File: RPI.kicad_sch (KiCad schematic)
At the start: 29 parts, among them J1 Conn_01x02_Male, J2 GPIO, J3 Conn_02x12, J4 Conn_02x12, J5 Conn_01x06, J6 Conn_01x04, J7 Conn_01x03, J8 Conn_01x02, J9 Conn_01x02, Q1 BC856BDW1, Q1 IRF9540N, Q2 IRF9540N, SW1 SW_SPDT, SW2 SW_SPDT, U1 LM1085-ADJ

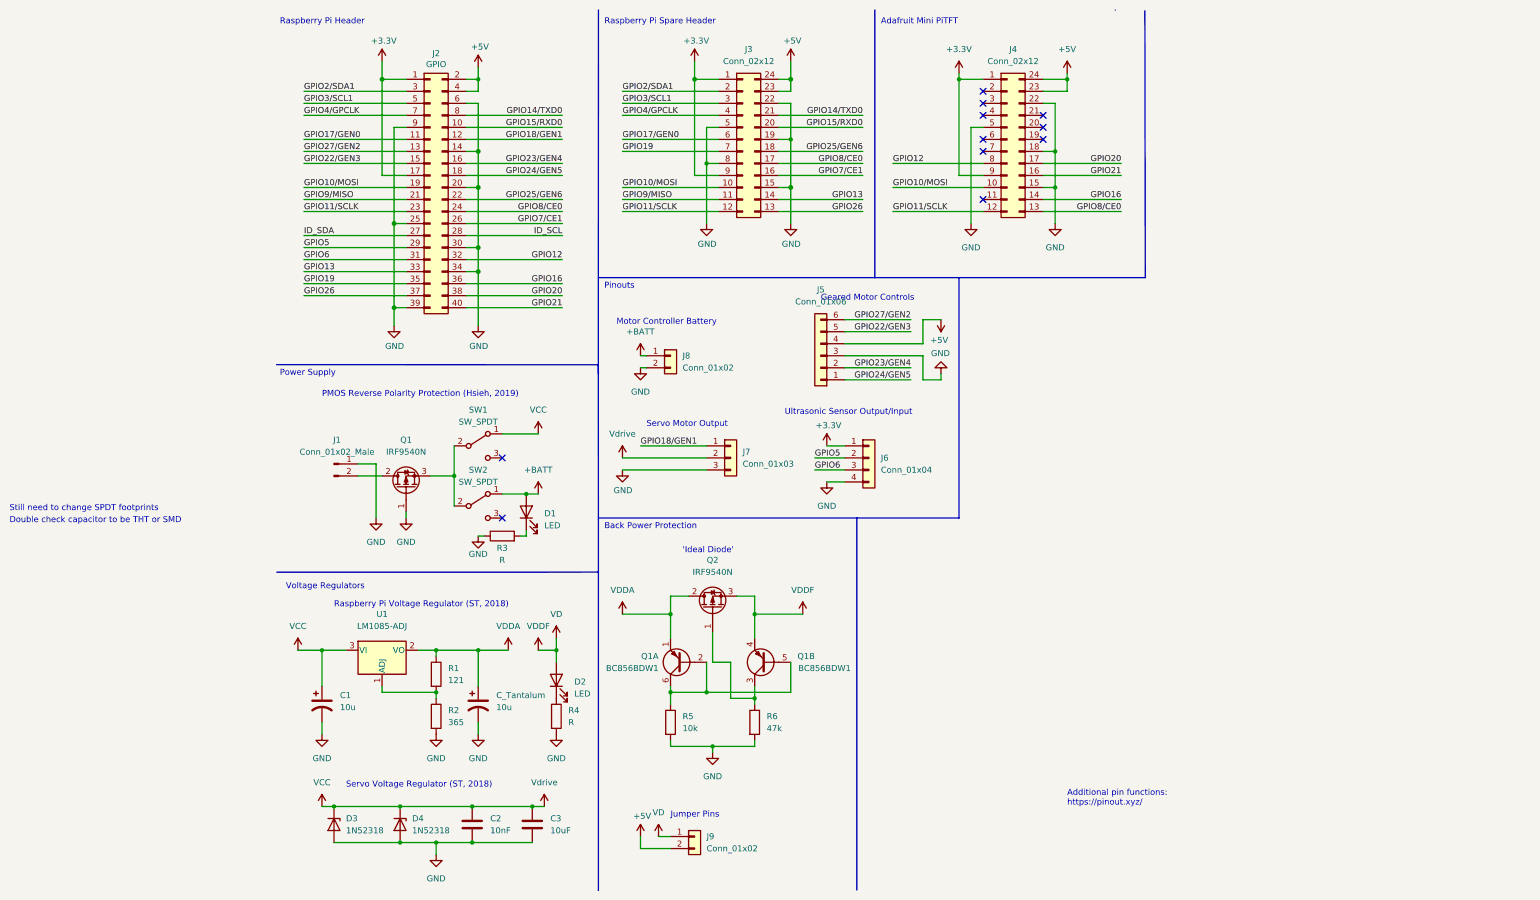
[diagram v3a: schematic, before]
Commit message: Completed Schematic, just need to edit footprints
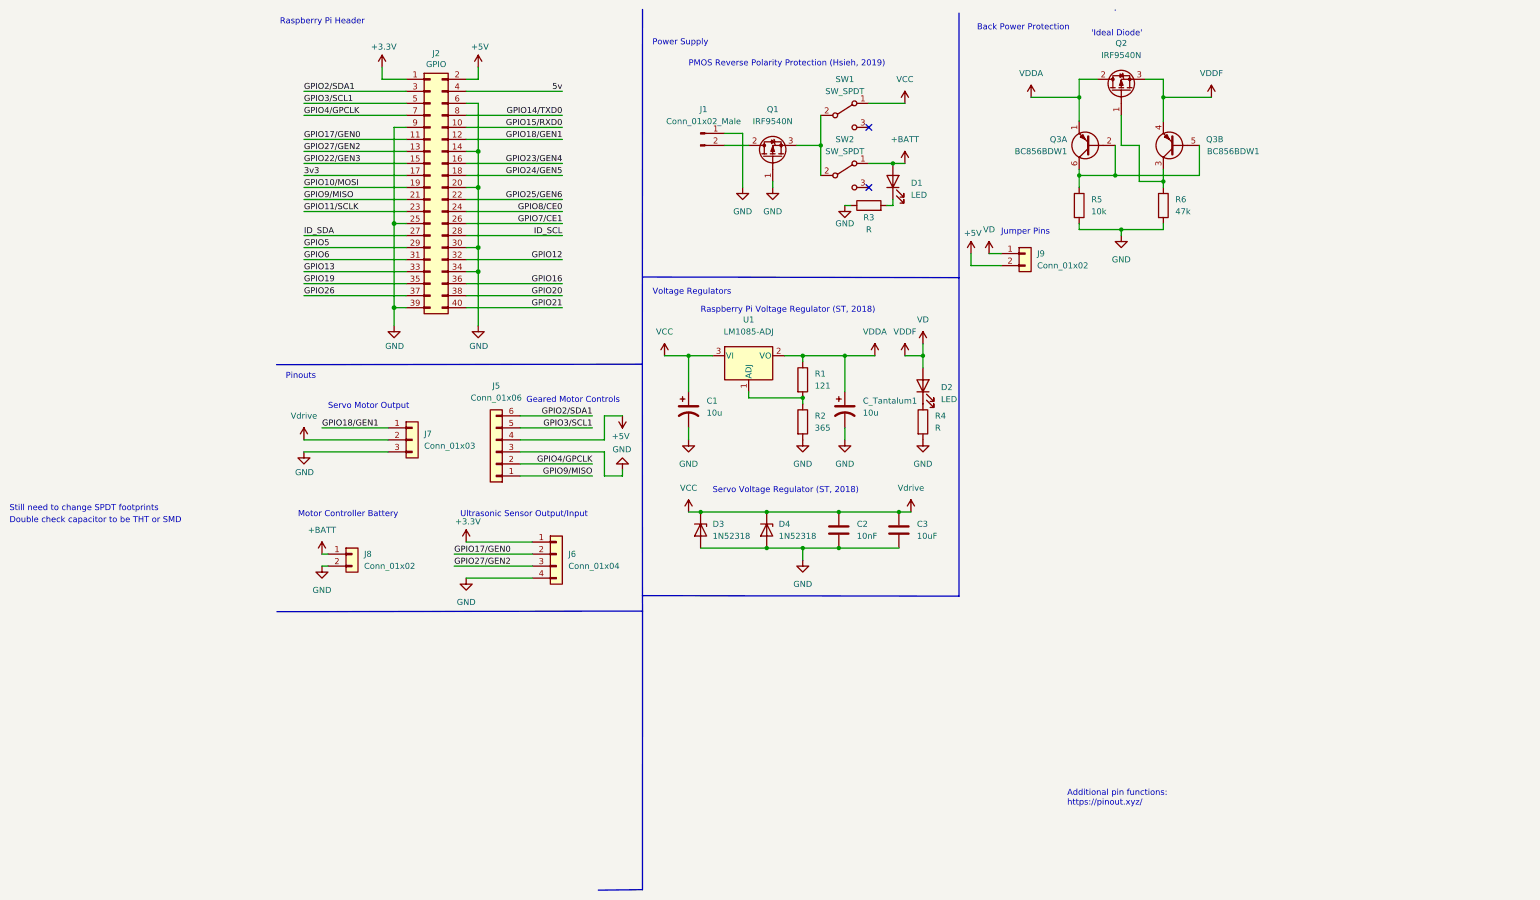
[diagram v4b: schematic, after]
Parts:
- removed J3, J4: Conn_02x12, Connector_PinSocket_2.54mm:PinSocket_2x12_P2.54mm_Vertical, symbol Connector_Generic:Conn_02x12_Counter_Clockwise
- C1: footprint (none) -> Capacitor_THT:CP_Radial_D5.0mm_P2.50mm
- C2, C3: footprint (none) -> Capacitor_SMD:C_0805_2012Metric_Pad1.18x1.45mm_HandSolder
- C_Tantalum1: renamed from C_Tantalum; footprint (none) -> Capacitor_Tantalum_SMD:CP_EIA-2012-12_Kemet-R_Pad1.30x1.05mm_HandSolder
- SW1, SW2: footprint (none) -> RPi_Hat:Switch_SPDT_Jaycar
- U1: footprint (none) -> RPi_Hat:LM1085-5.0
- renumbered Q1 to Q3
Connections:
- net +3V3: no longer J2.17 (Pin_17)
- net +5V: no longer J2.4 (Pin_4)
- net GPIO17/GEN0: now also J6.2 (Pin_2)
- net GPIO22/GEN3: no longer J5.5 (Pin_5)
- net GPIO23/GEN4: no longer J5.2 (Pin_2)
- net GPIO24/GEN5: no longer J5.1 (Pin_1)
- net GPIO27/GEN2: now also J6.3 (Pin_3); no longer J5.6 (Pin_6)
- net GPIO2/SDA1: now also J5.6 (Pin_6)
- net GPIO3/SCL1: now also J5.5 (Pin_5)
- net GPIO4/GPCLK: now also J5.2 (Pin_2)
- net GPIO5: no longer J6.2 (Pin_2)
- net GPIO6: no longer J6.3 (Pin_3)
- net GPIO9/MISO: now also J5.1 (Pin_1)
- new net 3v3: J2.17 (Pin_17)
- new net 5v: J2.4 (Pin_4)
- no-connect marks 11 -> 2
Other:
- note removed: "Adafruit Mini PiTFT"
- note removed: "Raspberry Pi Spare Header"
- moved on the sheet: C1, C2, C3, C_Tantalum1, D1, D2, D3, D4, J1, J5, J6, J7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

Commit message: Official completion (Maybe add Gerald in)
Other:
- note removed: "Double check capacitor to be THT or SMD"
- note removed: "Still need to change SPDT footprints"
- moved on the sheet: J7, J9, Q2, Q3A, Q3B, R5, R6

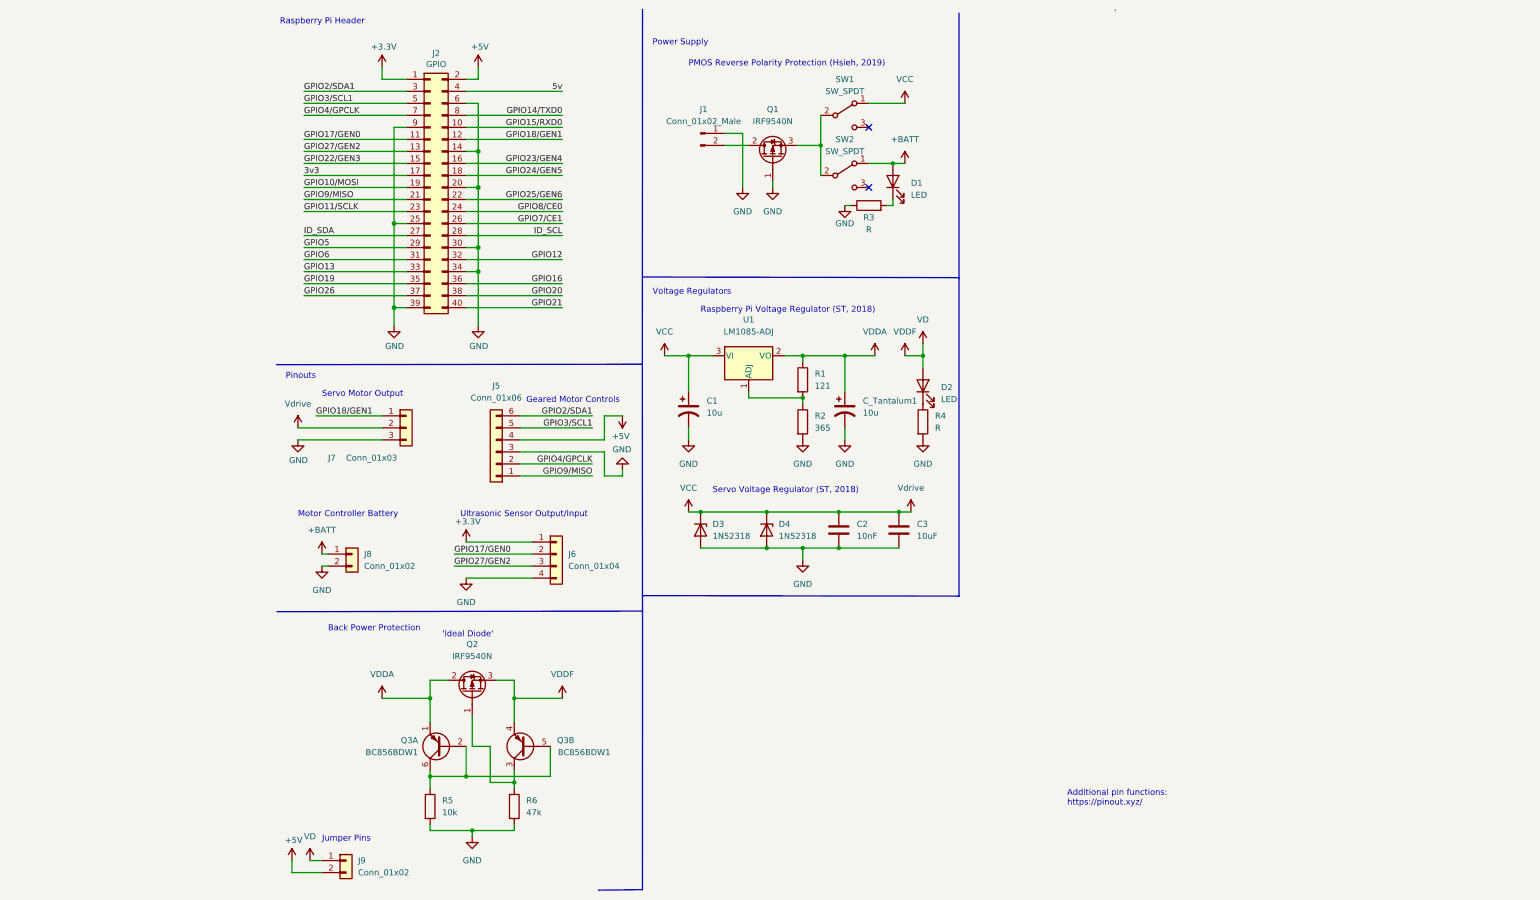
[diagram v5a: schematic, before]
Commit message: Added Fuse
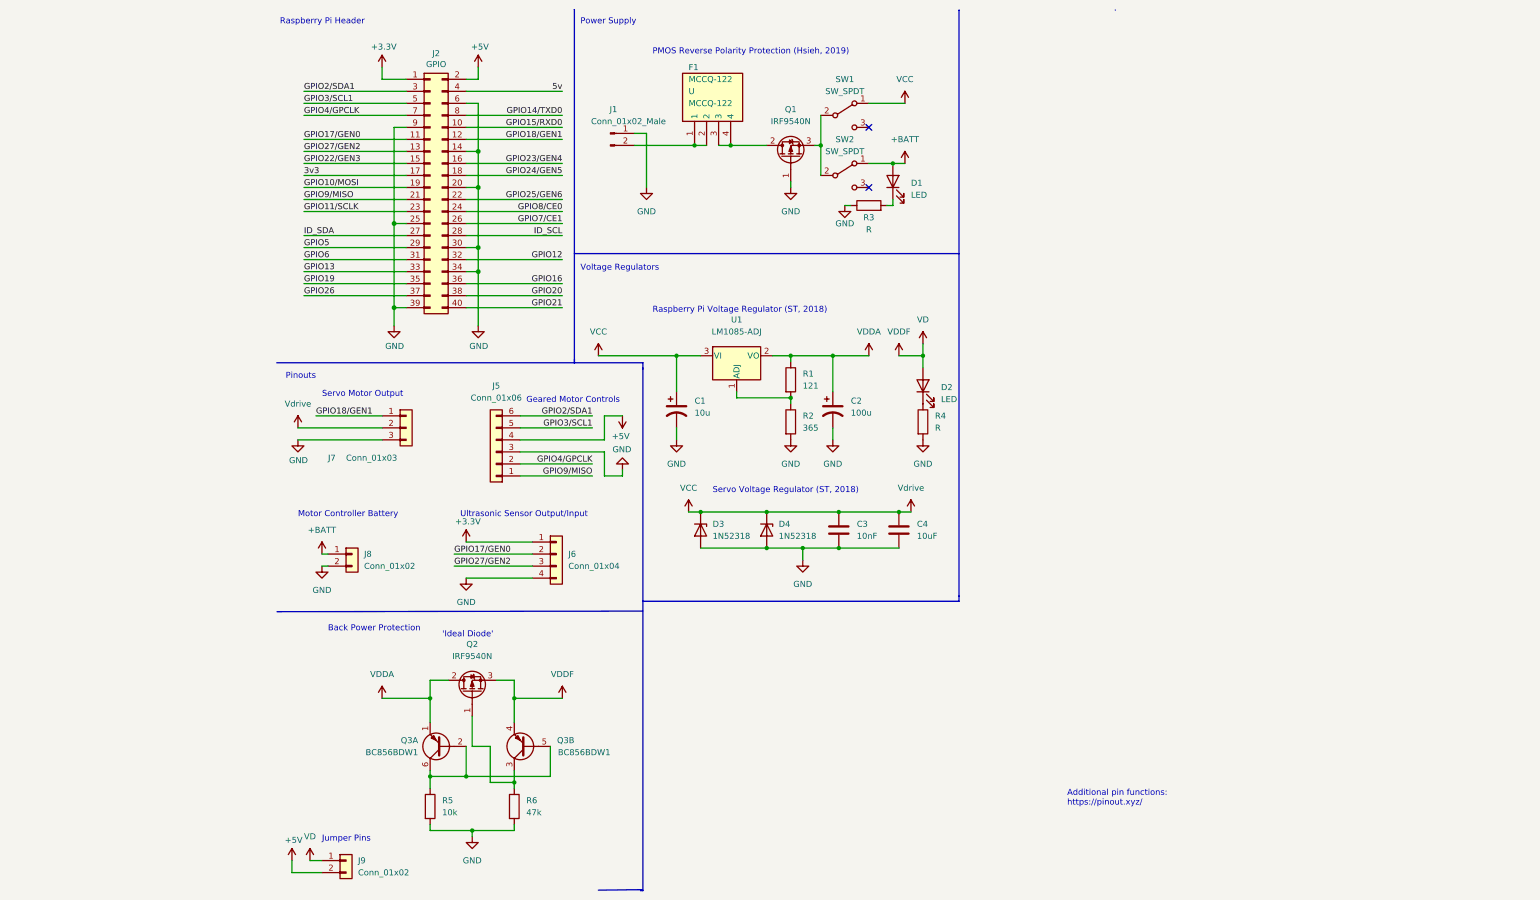
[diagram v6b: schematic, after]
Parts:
- added F1: MCCQ-122, RPi_Hat:MCCQ122, symbol MCQQ:MCCQ-122
- C2: renamed from C_Tantalum1; value 10u -> 100u
- renumbered C2 to C3, C3 to C4
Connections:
- net at Q1.2 (D): now also F1.3, F1.4; no longer J1.2 (Pin_2)
- new net: F1.1, F1.2, J1.2 (Pin_2)
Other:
- moved on the sheet: C1, C2, J1, Q1, R1, R2, U1

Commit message: fixed up using Fab ruleset and Matt's input
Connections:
- net 5v is gone; now on net +5V: J2.4 (Pin_4)
- net +5V: no longer J5.4 (Pin_4)
- no-connect marks 2 -> 3
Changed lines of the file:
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@@
   (junction (at 115.57 118.11) (diameter 0) (color 0 0 0 0)
   )
+  (junction (at 54.61 26.67) (diameter 0) (color 0 0 0 0)
+  )
   (junction (at 52.07 173.99) (diameter 0) (color 0 0 0 0)
   )
@@
   (junction (at 107.95 40.64) (diameter 0) (color 0 0 0 0)
   )
+  (no_connect (at 85.09 97.79))
   (no_connect (at 137.16 36.83))
   (no_connect (at 137.16 49.53))
@@
     (stroke (width 0) (type default) (color 0 0 0 0))
   )
+  (wire (pts (xy 54.61 26.67) (xy 54.61 29.21))
+    (stroke (width 0) (type default) (color 0 0 0 0))
+  )
   (wire (pts (xy 22.86 127) (xy 21.59 127))
     (stroke (width 0) (type default) (color 0 0 0 0))
@@
     (stroke (width 0) (type solid) (color 0 0 0 0))
   )
-  (wire (pts (xy 52.07 29.21) (xy 72.39 29.21))
+  (wire (pts (xy 52.07 29.21) (xy 54.61 29.21))
     (stroke (width 0) (type default) (color 0 0 0 0))
   )
@@
   (label "3v3" (at 17.78 46.99 0)
     (effects (font (size 1.27 1.27)) (justify left bottom))
-  )
-  (label "5v" (at 72.39 29.21 180)
-    (effects (font (size 1.27 1.27)) (justify right bottom))
   )
   (label "GPIO12" (at 72.39 64.77 180)
@@
     (pin "2")
   )
-  (symbol (lib_id "power:+5V") (at 85.09 97.79 180) (unit 1)
-    (in_bom yes) (on_board yes)
-    (property "Reference" "#PWR0134" (id 0) (at 85.09 93.98 0)
-      (effects (font (size 1.27 1.27)) hide)
-    )
-    (property "Value" "+5V" (id 1) (at 84.7217 102.1144 0))
-    (property "Footprint" "" (id 2) (at 85.09 97.79 0))
-    (property "Datasheet" "" (id 3) (at 85.09 97.79 0))
-    (pin "1")
-  )
   (symbol (lib_id "Connector_Generic:Conn_01x02") (at 27.94 127 0) (unit 1)
     (in_bom yes) (on_board yes) (fields_autoplaced)
@@
       (reference "#PWR0125") (unit 1) (value "VDDF") (footprint "")
     )
-    (path "/b7bb4b51-e6be-42d1-9291-16631afa1e6b"
-      (reference "#PWR0134") (unit 1) (value "+5V") (footprint "")
-    )
     (path "/cdb3726e-c1bd-48e1-b03b-f9a827b4631d"

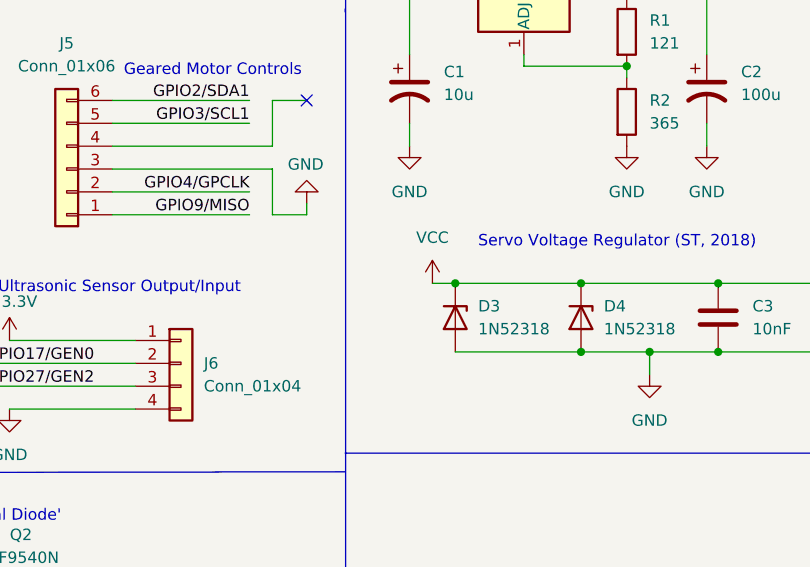
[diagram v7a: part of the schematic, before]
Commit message: Added load resistor & updated footprints
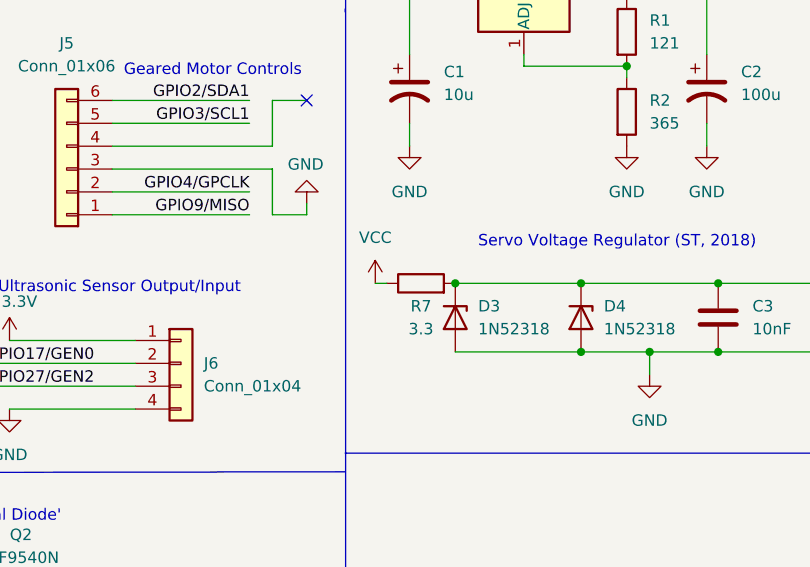
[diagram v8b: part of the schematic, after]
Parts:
- added R7: 3.3, Resistor_THT:R_Axial_DIN0207_L6.3mm_D2.5mm_P10.16mm_Horizontal, symbol Device:R
- J8: footprint Connector_PinSocket_2.54mm:PinSocket_1x02_P2.54mm_Vertical -> RPi_Hat:TE_282836-2
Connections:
- net VCC: now also R7.1; no longer C3.1, C4.1, D3.1 (K), D4.1 (K), J7.2 (Pin_2)
- new net Vdrive: C3.1, C4.1, D3.1 (K), D4.1 (K), J7.2 (Pin_2), R7.2
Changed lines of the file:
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@@
   (junction (at 96.52 85.09) (diameter 0) (color 0 0 0 0)
   )
+  (junction (at 130.81 125.73) (diameter 0) (color 0 0 0 0)
+  )
+  (junction (at 100.33 40.64) (diameter 0) (color 0 0 0 0)
+  )
+  (junction (at 115.57 125.73) (diameter 0) (color 0 0 0 0)
+  )
+  (junction (at 54.61 62.23) (diameter 1.016) (color 0 0 0 0)
+  )
+  (junction (at 44.45 173.99) (diameter 0) (color 0 0 0 0)
+  )
+  (junction (at 129.54 85.09) (diameter 0) (color 0 0 0 0)
+  )
+  (junction (at 54.61 49.53) (diameter 1.016) (color 0 0 0 0)
+  )
+  (junction (at 130.81 118.11) (diameter 0) (color 0 0 0 0)
+  )
   (junction (at 101.6 118.11) (diameter 0) (color 0 0 0 0)
-  )
-  (junction (at 130.81 125.73) (diameter 0) (color 0 0 0 0)
-  )
-  (junction (at 100.33 40.64) (diameter 0) (color 0 0 0 0)
-  )
-  (junction (at 115.57 125.73) (diameter 0) (color 0 0 0 0)
-  )
-  (junction (at 54.61 62.23) (diameter 1.016) (color 0 0 0 0)
-  )
-  (junction (at 44.45 173.99) (diameter 0) (color 0 0 0 0)
-  )
-  (junction (at 129.54 85.09) (diameter 0) (color 0 0 0 0)
-  )
-  (junction (at 54.61 49.53) (diameter 1.016) (color 0 0 0 0)
-  )
-  (junction (at 130.81 118.11) (diameter 0) (color 0 0 0 0)
   )
   (junction (at 107.95 40.64) (diameter 0) (color 0 0 0 0)
@@
     (stroke (width 0) (type default) (color 0 0 0 0))
   )
-  (wire (pts (xy 99.06 118.11) (xy 101.6 118.11))
-    (stroke (width 0) (type default) (color 0 0 0 0))
-  )
   (wire (pts (xy 81.28 102.87) (xy 63.5 102.87))
     (stroke (width 0) (type default) (color 0 0 0 0))
@@
   (wire (pts (xy 39.37 67.31) (xy 17.78 67.31))
     (stroke (width 0) (type solid) (color 0 0 0 0))
+  )
+  (wire (pts (xy 92.71 118.11) (xy 93.98 118.11))
+    (stroke (width 0) (type default) (color 0 0 0 0))
   )
   (wire (pts (xy 54.61 62.23) (xy 52.07 62.23))
@@
     (pin "1")
   )
+  (symbol (lib_id "Device:R") (at 97.79 118.11 90) (unit 1)
+    (in_bom yes) (on_board yes)
+    (property "Reference" "R7" (id 0) (at 97.79 120.65 90))
+    (property "Value" "3.3" (id 1) (at 97.79 123.19 90))
+    (property "Footprint" "Resistor_THT:R_Axial_DIN0207_L6.3mm_D2.5mm_P10.16mm_Horizontal" (id 2) (at 97.79 119.888 90)
+      (effects (font (size 1.27 1.27)) hide)
+    )
+    (property "Datasheet" "~" (id 3) (at 97.79 118.11 0)
+      (effects (font (size 1.27 1.27)) hide)
+    )
+    (pin "1")
+    (pin "2")
+  )
   (symbol (lib_id "Transistor_FET:IRF9540N") (at 120.65 43.18 90) (unit 1)
     (in_bom yes) (on_board yes) (fields_autoplaced)
@@
       (effects (font (size 1.27 1.27)) (justify left))
     )
-    (property "Footprint" "Connector_PinSocket_2.54mm:PinSocket_1x02_P2.54mm_Vertical" (id 2) (at 27.94 127 0)
+    (property "Footprint" "RPi_Hat:TE_282836-2" (id 2) (at 27.94 127 0)
       (effects (font (size 1.27 1.27)) hide)
     )
@@
     (pin "2")
   )
-  (symbol (lib_id "power:VCC") (at 99.06 118.11 0) (unit 1)
-    (in_bom yes) (on_board yes) (fields_autoplaced)
-    (property "Reference" "#PWR0102" (id 0) (at 99.06 121.92 0)
-      (effects (font (size 1.27 1.27)) hide)
-    )
-    (property "Value" "VCC" (id 1) (at 99.06 113.03 0))
-    (property "Footprint" "" (id 2) (at 99.06 118.11 0)
-      (effects (font (size 1.27 1.27)) hide)
-    )
-    (property "Datasheet" "" (id 3) (at 99.06 118.11 0)
+  (symbol (lib_id "power:VCC") (at 92.71 118.11 0) (unit 1)
+    (in_bom yes) (on_board yes) (fields_autoplaced)
+    (property "Reference" "#PWR0102" (id 0) (at 92.71 121.92 0)
+      (effects (font (size 1.27 1.27)) hide)
+    )
+    (property "Value" "VCC" (id 1) (at 92.71 113.03 0))
+    (property "Footprint" "" (id 2) (at 92.71 118.11 0)
+      (effects (font (size 1.27 1.27)) hide)
+    )
+    (property "Datasheet" "" (id 3) (at 92.71 118.11 0)
       (effects (font (size 1.27 1.27)) hide)
     )
@@
     )
     (path "/be2555fb-5ae5-40f2-b536-3b75ec680a50"
-      (reference "J8") (unit 1) (value "Conn_01x02") (footprint "Connector_PinSocket_2.54mm:PinSocket_1x02_P2.54mm_Vertical")
+      (reference "J8") (unit 1) (value "Conn_01x02") (footprint "RPi_Hat:TE_282836-2")
     )
     (path "/af09e953-dedc-43a3-8e20-fcf37551f0ba"
@@
       (reference "R6") (unit 1) (value "47k") (footprint "Resistor_SMD:R_0805_2012Metric_Pad1.20x1.40mm_HandSolder")
     )
+    (path "/991e23f9-0d19-4616-af5a-f5d26c0e2123"
+      (reference "R7") (unit 1) (value "3.3") (footprint "Resistor_THT:R_Axial_DIN0207_L6.3mm_D2.5mm_P10.16mm_Horizontal")
+    )
     (path "/d096b0ce-6e92-4b87-8cd2-4483e65f79e1"
